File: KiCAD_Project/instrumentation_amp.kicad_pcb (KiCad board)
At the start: 2 copper layers, 63.5 x 48.3 mm, 73 parts, among them J1 SPDT_SOLDER, J2 SPDT_SOLDER, J3 SPDT_SOLDER, J4 SPDT_SOLDER, P1 +VIN, P10 TXDR -OUT 2, P11 +15VDC, P12 +15VDC, P13 +15VDC, P14 -15VDC, P15 -15VDC, P16 -15VDC, P17 GND, P18 GND, P19 GND, P2 -VIN, P20 GND, P3 TXDR -IN 1, P4 TXDR -IN 1, P5 TXDR -IN 2, P6 TXDR -IN 2, P7 TXDR -OUT 1, P8 TXDR -OUT 1, P9 TXDR -OUT 2, U1 LM7815CT, U2 LM7915CT, U3 INA128, U4 INA128

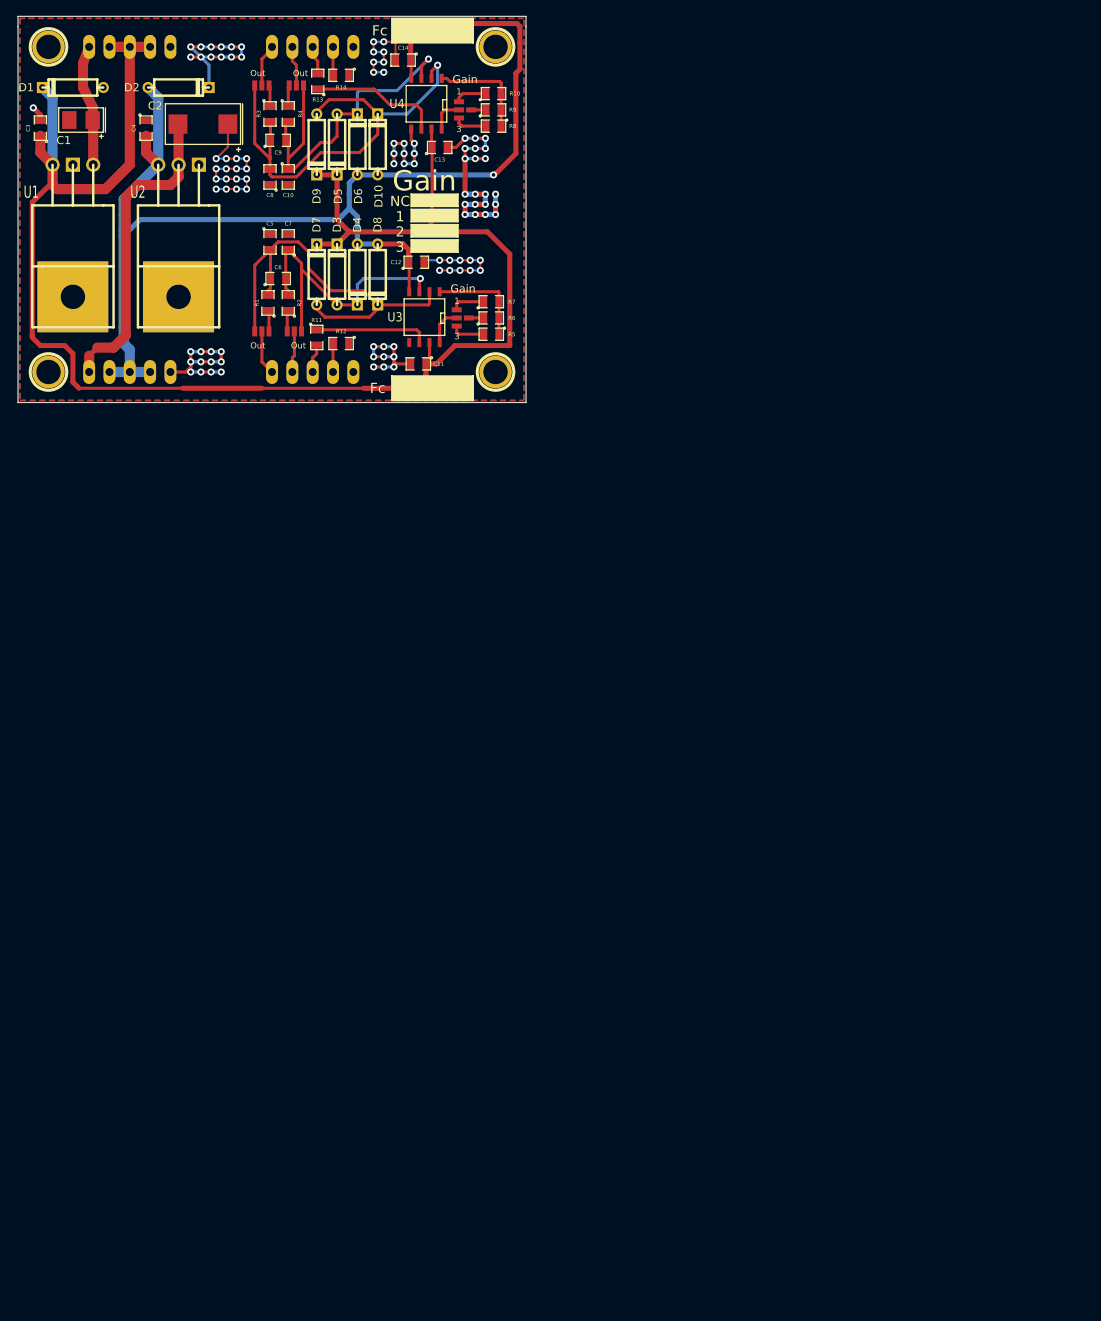
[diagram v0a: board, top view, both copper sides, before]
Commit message: Change jumpers for better operation and rework the layout
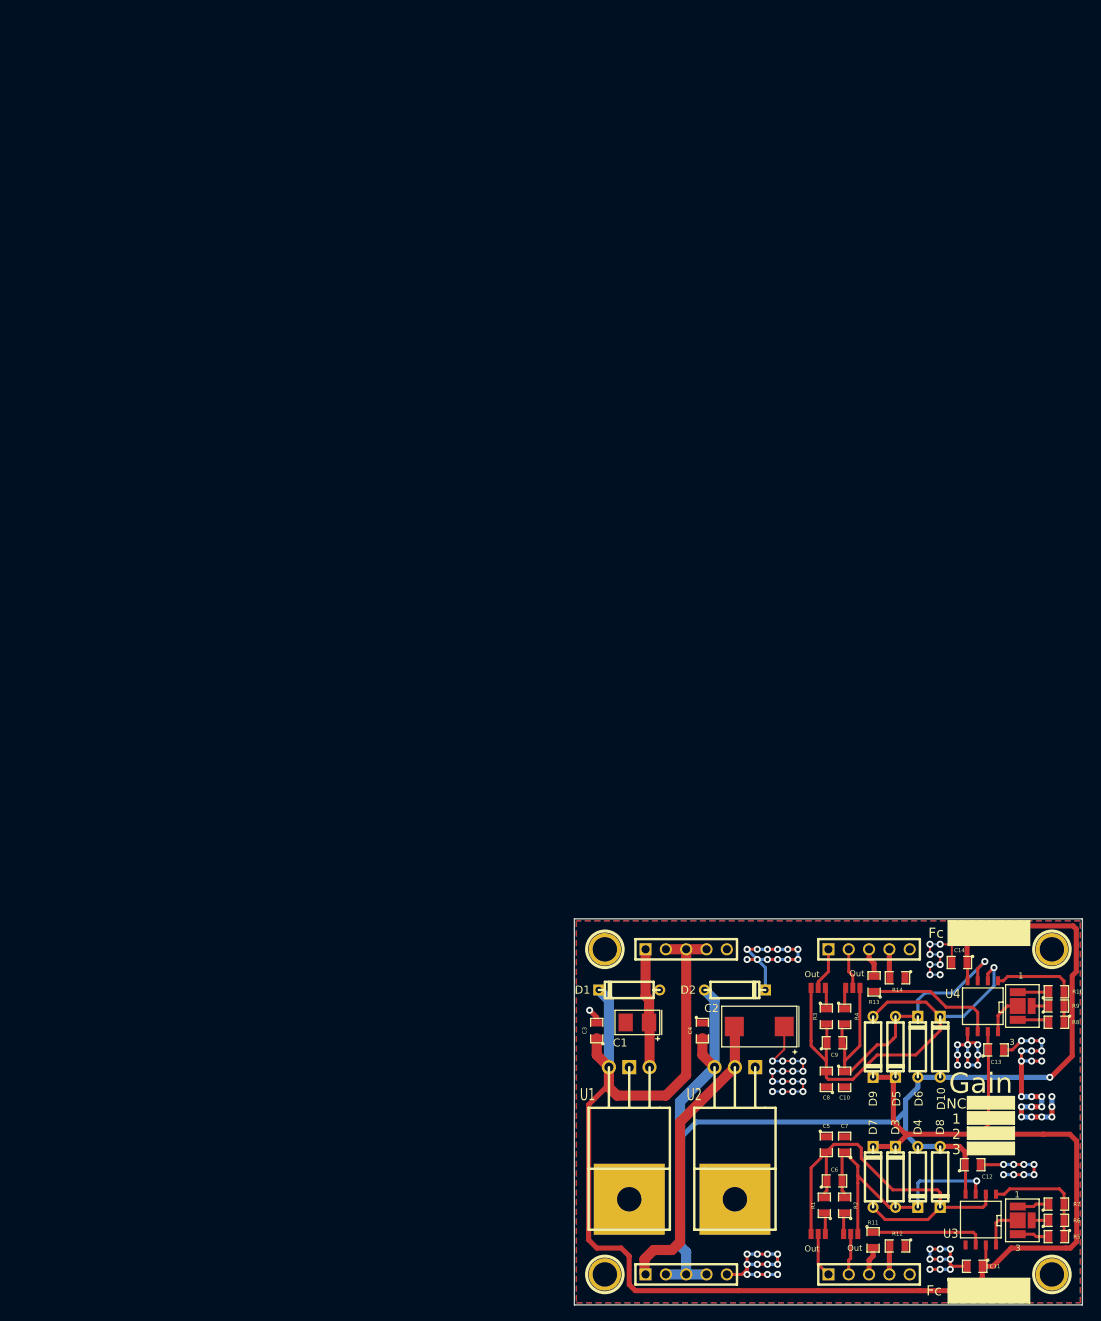
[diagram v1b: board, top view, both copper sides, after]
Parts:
- removed Gain (x2): SP3T_SOLDER, SP3T
- removed P10, P9: TXDR -OUT 2, 1pinhead
- removed P11, P12, P13: +15VDC, 1pinhead
- removed P14, P15, P16: -15VDC, 1pinhead
- removed P17, P18, P19, P20: GND, 1pinhead
- removed P5, P6: TXDR -IN 2, 1pinhead
- removed P7, P8: TXDR -OUT 1, 1pinhead
- added J5: SP3T_SOLDER, Solder_SPTT, F.Cu at (184.7, 164.5)
- added J6: SP3T_SOLDER, Solder_SPTT, F.Cu at (184.7, 137.7)
- P1: value +VIN -> CONN_5; footprint 1pinhead -> PIN_ARRAY_5x1
- P2: value -VIN -> CONN_5; footprint 1pinhead -> PIN_ARRAY_5x1
- P3, P4: value TXDR -IN 1 -> CONN_5; footprint 1pinhead -> PIN_ARRAY_5x1
- R10, R7: value 499 -> 511
- R6, R9: value 5.49K -> 5.62K
- moved P2 135.3 mm to (143.2, 171.2)
- moved P1 135.3 mm to (143.2, 130.6)
- moved P3 135.3 mm to (166.1, 171.2)
- moved R5 133.1 mm to (189.5, 166.5)
- moved R6 133.1 mm to (189.5, 164.5)
- moved R7 133.1 mm to (189.5, 162.4)
- moved D10 132.9 mm to (175.0, 142.8)
- moved D8 132.9 mm to (175.0, 159.0)
- moved D4 132.8 mm to (172.2, 159.0)
- moved D6 132.8 mm to (172.2, 142.8)
- moved D3 132.7 mm to (169.4, 159.0)
- moved D5 132.7 mm to (169.4, 142.8)
- moved J1 132.5 mm to (159.7, 166.2)
- moved J2 132.5 mm to (163.8, 166.2)
- moved 1PIN 132.5 mm to (188.9, 171.2)
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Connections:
- C11 pad 1: +15V -> VDD
- C12 pad 1: -15V -> VSS
- C13 pad 1: +15V -> VDD
- C14 pad 1: -15V -> VSS
- C3 pad 1: +15V -> VDD
- C4 pad 2: -15V -> VSS
- D1 pad 2: +15V -> VDD
- D10 pad 1: -15V -> VSS
- D2 pad 1: -15V -> VSS
- D3 pad 2: +15V -> VDD
- D4 pad 1: -15V -> VSS
- D5 pad 2: +15V -> VDD
- D6 pad 1: -15V -> VSS
- D7 pad 2: +15V -> VDD
- D8 pad 1: -15V -> VSS
- D9 pad 2: +15V -> VDD
- J1 pad 1: N-0000031 (its old number) -> /A -IN
- J2 pad 1: N-0000033 (its old number) -> /A +IN
- J3 pad 1: N-0000017 -> /B -IN
- J4 pad 1: N-0000019 -> /B +IN
- P3 pad 1: N-0000031 (its old number) -> /A -IN
- P4 pad 1: N-0000033 (its old number) -> /B -IN
- R11 pad 2: N-0000023 (its old number) -> /A +OUT
- R12 pad 2: N-0000025 -> /A -OUT
- R13 pad 2: N-000001 -> /B +OUT
- R14 pad 2: N-000003 (its old number) -> /B -OUT
- U1 pad 3: +15V -> VDD
- U2 pad 3: -15V -> VSS
- U3 pad 4: -15V -> VSS
- U3 pad 7: +15V -> VDD
- U4 pad 4: -15V -> VSS
- U4 pad 7: +15V -> VDD
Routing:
- net +15V: track 228.1 -> 0.00 mm
- net VDD: track 0.00 -> 226.9 mm
- net -15V: track 159.1 -> 0.00 mm, vias 1 -> 0
- net VSS: track 0.00 -> 157.1 mm, vias 0 -> 1
- net (no net): track 13.3 -> 0.25 mm, vias 10 -> 0
- net GND: track 134.8 -> 147.3 mm, vias 88 -> 96
- net /A +OUT: track 0.00 -> 7.14 mm
- net /B +OUT: track 0.00 -> 5.68 mm
- net /A -IN: track 0.00 -> 5.61 mm
- net N-0000031 (its old number): track 5.61 -> 0.00 mm
- net /B -IN: track 0.00 -> 5.36 mm
- net N-0000017: track 5.35 -> 0.00 mm
- net /A +IN: track 0.00 -> 5.19 mm
- net N-0000033 (its old number): track 5.19 -> 0.00 mm
- net /B +IN: track 0.00 -> 5.04 mm
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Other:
- board text added: "+Vin"
- board text added: "+Vout"
- board text added: "-Vin"
- board text added: "-Vout"
- board text added: "Rev. B 2014"
- board text removed: "+15 VDC"
- board text removed: "+VIN"
- board text removed: "-15 VDC"
- board text removed: "-VIN"
